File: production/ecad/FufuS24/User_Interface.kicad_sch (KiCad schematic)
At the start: 3 parts, among them J3 HDMI_A, J4 USB_B_Micro

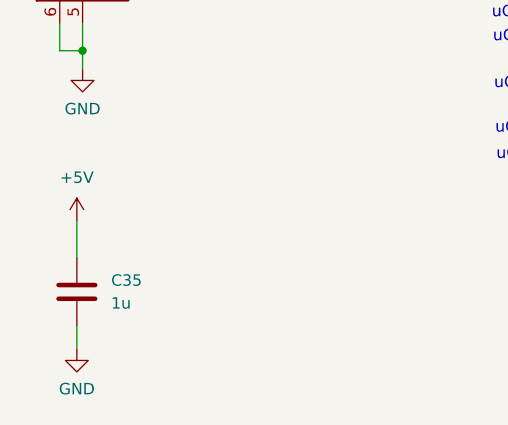
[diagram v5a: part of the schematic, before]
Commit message: Update User_Interface.kicad_sch
Removed decoupling cap for 5V on UI it might be redundant
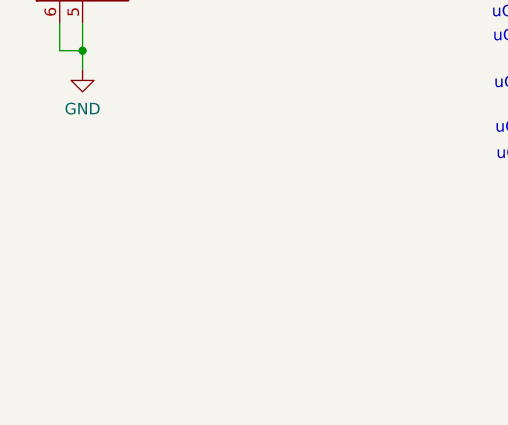
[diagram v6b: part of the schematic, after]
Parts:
- removed C35: 1u, symbol Device:C
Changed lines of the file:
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@@
-    (stroke (width 0) (type default))
-  )
-  (wire (pts (xy 110.617 123.317) (xy 110.617 125.857))
-    (stroke (width 0) (type default))
-  )
-  (wire (pts (xy 110.617 111.633) (xy 110.617 115.697))
     (stroke (width 0) (type default))
   )
@@
     (property "Intersheetrefs" "${INTERSHEET_REFS}" (at 168.9365 91.059 0)
       (effects (font (size 1.27 1.27)) (justify right) hide)
-    )
-  )
-  (symbol (lib_id "power:GND") (at 110.617 125.857 0) (unit 1)
-    (in_bom yes) (on_board yes) (dnp no) (fields_autoplaced)
-    (property "Reference" "#PWR069" (at 110.617 132.207 0)
-      (effects (font (size 1.27 1.27)) hide)
-    )
-    (property "Value" "GND" (at 110.617 130.302 0)
-      (effects (font (size 1.27 1.27)))
-    )
-    (property "Footprint" "" (at 110.617 125.857 0)
-      (effects (font (size 1.27 1.27)) hide)
-    )
-    (property "Datasheet" "" (at 110.617 125.857 0)
-      (effects (font (size 1.27 1.27)) hide)
-    )
-    (pin "1")
-    (instances
-      (project "FufuS24"
-        (path "/c4c3980b-c8c0-435e-abdc-bbed2349d7ac/876a98ff-842e-4695-a72d-b69ed233d34f"
-          (reference "#PWR069") (unit 1)
-        )
-      )
     )
   )
@@
         )
       )
-    )
-  )
-  (symbol (lib_id "power:+5V") (at 110.617 111.633 0) (unit 1)
-    (in_bom yes) (on_board yes) (dnp no) (fields_autoplaced)
-    (property "Reference" "#PWR066" (at 110.617 115.443 0)
-      (effects (font (size 1.27 1.27)) hide)
-    )
-    (property "Value" "+5V" (at 110.617 106.807 0)
-      (effects (font (size 1.27 1.27)))
-    )
-    (property "Footprint" "" (at 110.617 111.633 0)
-      (effects (font (size 1.27 1.27)) hide)
-    )
-    (property "Datasheet" "" (at 110.617 111.633 0)
-      (effects (font (size 1.27 1.27)) hide)
-    )
-    (pin "1")
-    (instances
-      (project "FufuS24"
-        (path "/c4c3980b-c8c0-435e-abdc-bbed2349d7ac/876a98ff-842e-4695-a72d-b69ed233d34f"
-          (reference "#PWR066") (unit 1)
-        )
-      )
-    )
-  )
-  (symbol (lib_id "Device:C") (at 110.617 119.507 0) (unit 1)
-    (in_bom yes) (on_board yes) (dnp no) (fields_autoplaced)
-    (property "Reference" "C35" (at 114.427 118.237 0)
-      (effects (font (size 1.27 1.27)) (justify left))
-    )
-    (property "Value" "1u" (at 114.427 120.777 0)
-      (effects (font (size 1.27 1.27)) (justify left))
-    )
-    (property "Footprint" "" (at 111.5822 123.317 0)
-      (effects (font (size 1.27 1.27)) hide)
-    )
-    (property "Datasheet" "~" (at 110.617 119.507 0)
-      (effects (font (size 1.27 1.27)) hide)
-    )
-    (pin "1")
-    (pin "2")
-    (instances
-      (project "FufuS24"
-        (path "/c4c3980b-c8c0-435e-abdc-bbed2349d7ac/876a98ff-842e-4695-a72d-b69ed233d34f"
-          (reference "C35") (unit 1)
-        )
-      )

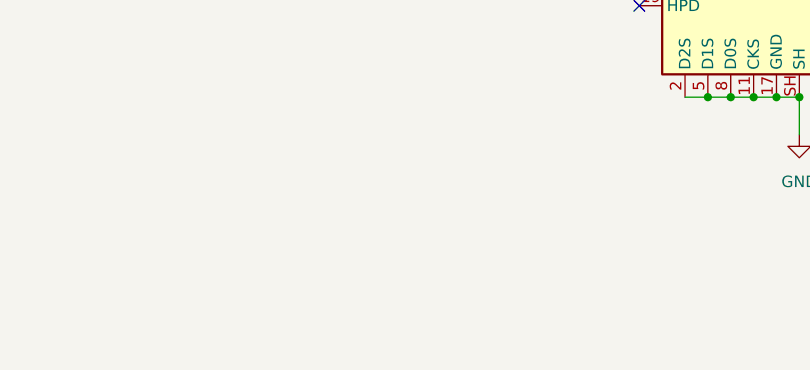
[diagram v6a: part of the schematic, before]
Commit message: Design review changes
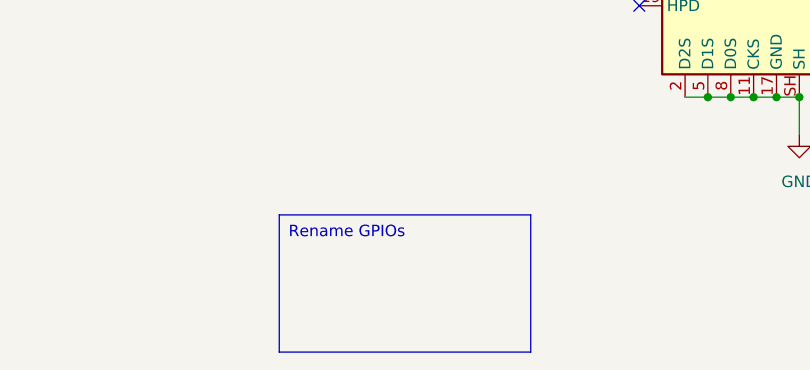
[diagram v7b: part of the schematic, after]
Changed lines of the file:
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@@
     (stroke (width 0) (type default))
+  )
+  (text_box "Rename GPIOs"
+    (at 140.97 134.62 0) (size 27.94 15.24)
+    (stroke (width 0) (type default))
+    (fill (type none))
+    (effects (font (size 1.27 1.27)) (justify left top))
   )
   (text "uC_DVI_D1-" (at 156.718 81.788 0)

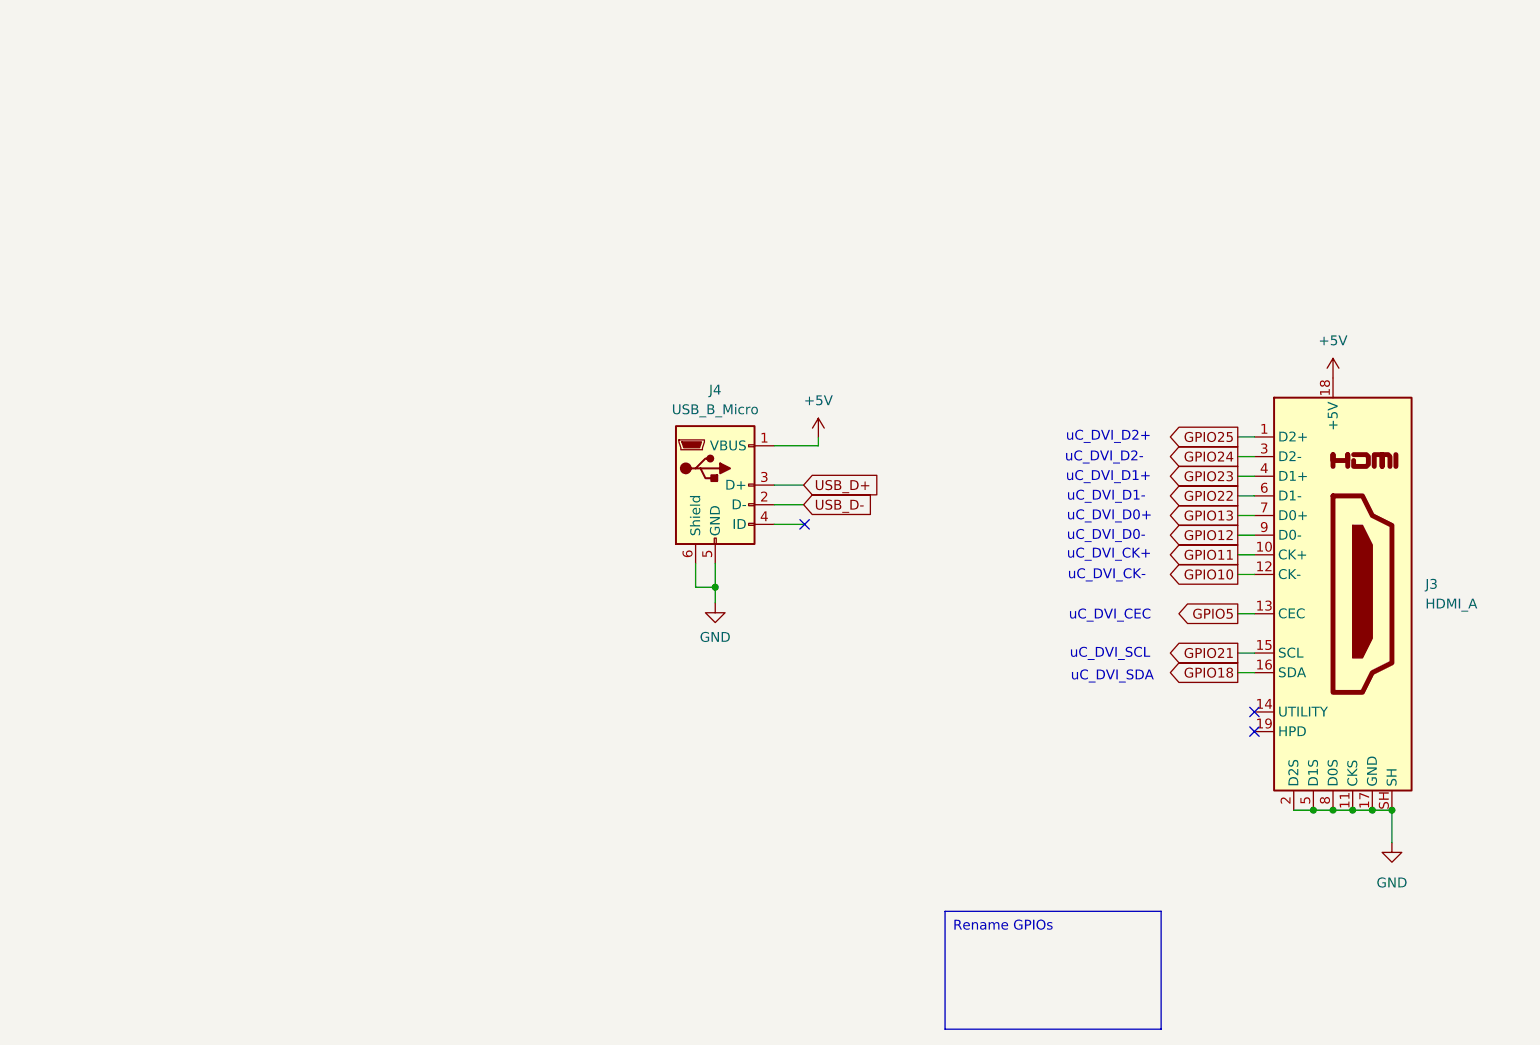
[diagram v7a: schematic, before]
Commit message: added resistors to HDMI
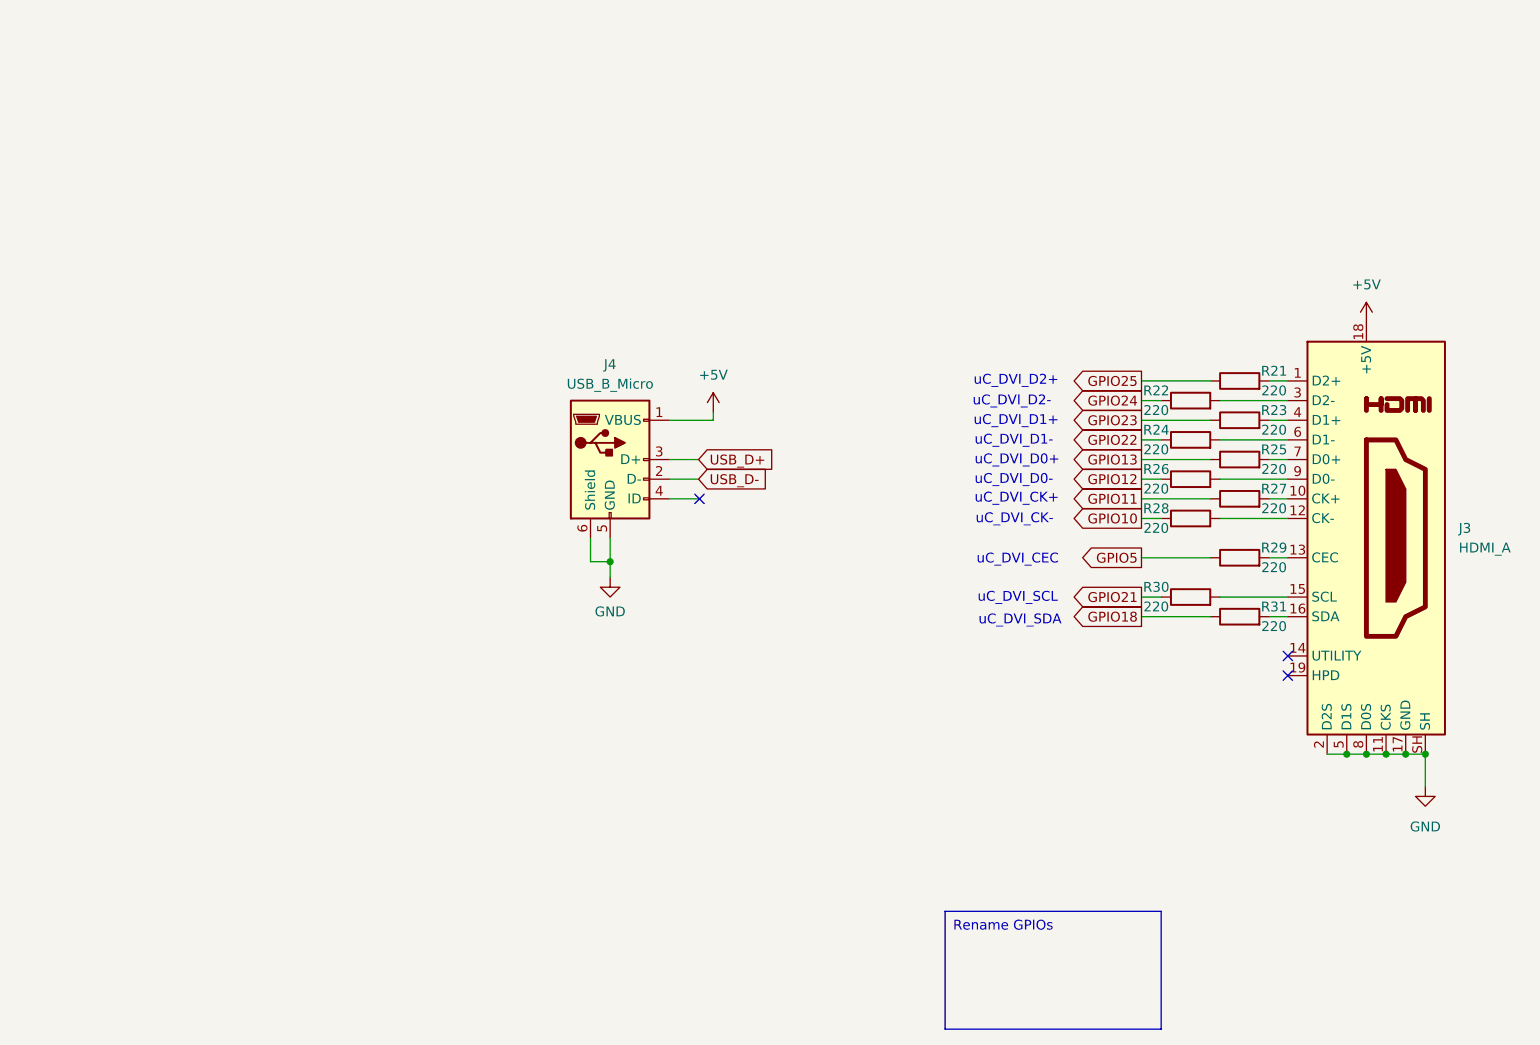
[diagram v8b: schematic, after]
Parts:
- added R21, R22, R23, R24, R25, R26, R27, R28, R29, R30, R31: 220, symbol Device:R
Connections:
- net GPIO10: now also R28.1; no longer J3.12 (CK-)
- net GPIO11: now also R27.1; no longer J3.10 (CK+)
- net GPIO12: now also R26.1; no longer J3.9 (D0-)
- net GPIO13: now also R25.1; no longer J3.7 (D0+)
- net GPIO18: now also R31.1; no longer J3.16 (SDA)
- net GPIO21: now also R30.1; no longer J3.15 (SCL)
- net GPIO22: now also R24.1; no longer J3.6 (D1-)
- net GPIO23: now also R23.1; no longer J3.4 (D1+)
- net GPIO24: now also R22.1; no longer J3.3 (D2-)
- net GPIO25: now also R21.1; no longer J3.1 (D2+)
- net GPIO5: now also R29.1; no longer J3.13 (CEC)
- new net: J3.7 (D0+), R25.2
- new net: J3.6 (D1-), R24.2
- new net: J3.13 (CEC), R29.2
- new net: J3.16 (SDA), R31.2
- new net: J3.15 (SCL), R30.2
- new net: J3.10 (CK+), R27.2
- new net: J3.4 (D1+), R23.2
- new net: J3.9 (D0-), R26.2
- new net: J3.1 (D2+), R21.2
- new net: J3.12 (CK-), R28.2
- new net: J3.3 (D2-), R22.2
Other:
- moved on the sheet: J3, J4
